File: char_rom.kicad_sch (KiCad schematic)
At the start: 3 parts, among them U20 2732, U20B1 '64 - '512, U20C1 '010 - '080

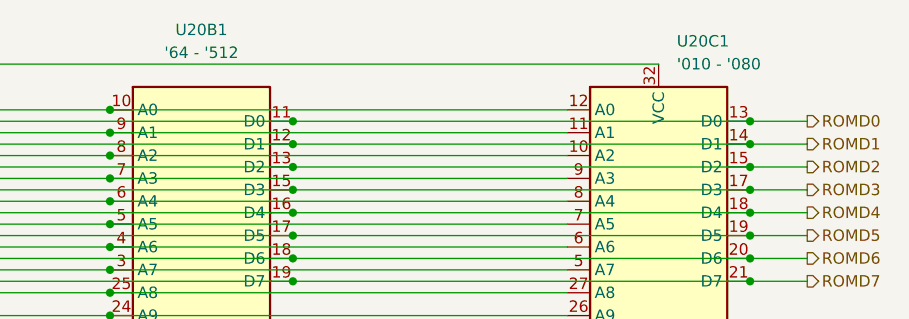
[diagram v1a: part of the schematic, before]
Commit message: rename alternate char rom footprints
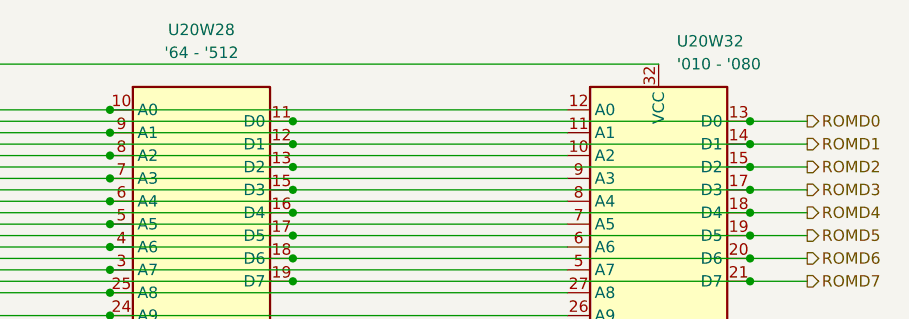
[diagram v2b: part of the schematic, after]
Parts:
- renumbered U20B1 to U20W28, U20C1 to U20W32
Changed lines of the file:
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@@
   (symbol (lib_id "Memory_EPROM:27C128") (at 137.16 78.74 0) (unit 1)
     (in_bom yes) (on_board yes) (fields_autoplaced)
-    (property "Reference" "U20B1" (id 0) (at 137.16 41.91 0))
+    (property "Reference" "U20W28" (id 0) (at 137.16 41.91 0))
     (property "Value" "'64 - '512" (id 1) (at 137.16 44.45 0))
     (property "Footprint" "Package_DIP:DIP-28_W15.24mm" (id 2) (at 137.16 73.66 0)
@@
   (symbol (lib_id "Memory_EPROM:27C020") (at 187.96 78.74 0) (unit 1)
     (in_bom yes) (on_board yes) (fields_autoplaced)
-    (property "Reference" "U20C1" (id 0) (at 189.9794 43.18 0)
+    (property "Reference" "U20W32" (id 0) (at 189.9794 43.18 0)
       (effects (font (size 1.27 1.27)) (justify left))
     )
